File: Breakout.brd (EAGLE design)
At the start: 42 x 45 mm, 11 parts

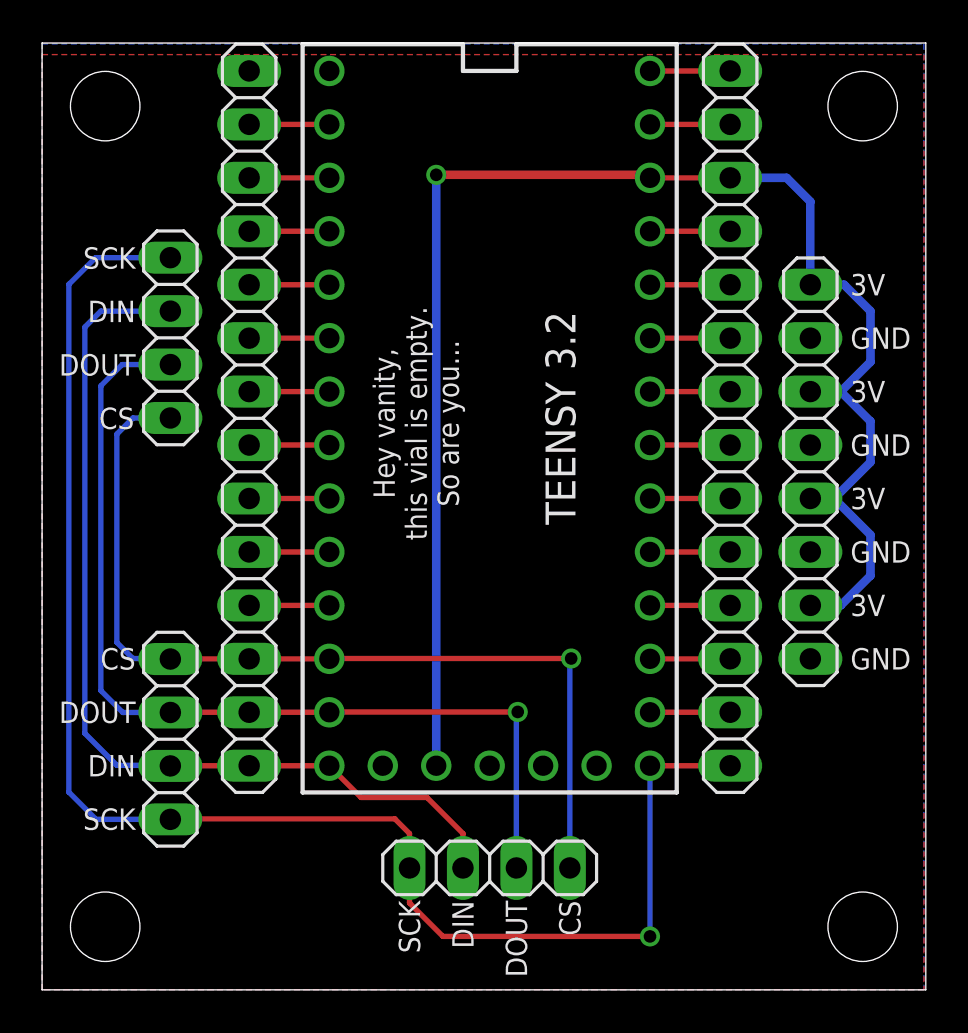
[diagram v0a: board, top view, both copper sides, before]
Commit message: Nudge layout to fit more squarely on mil grid
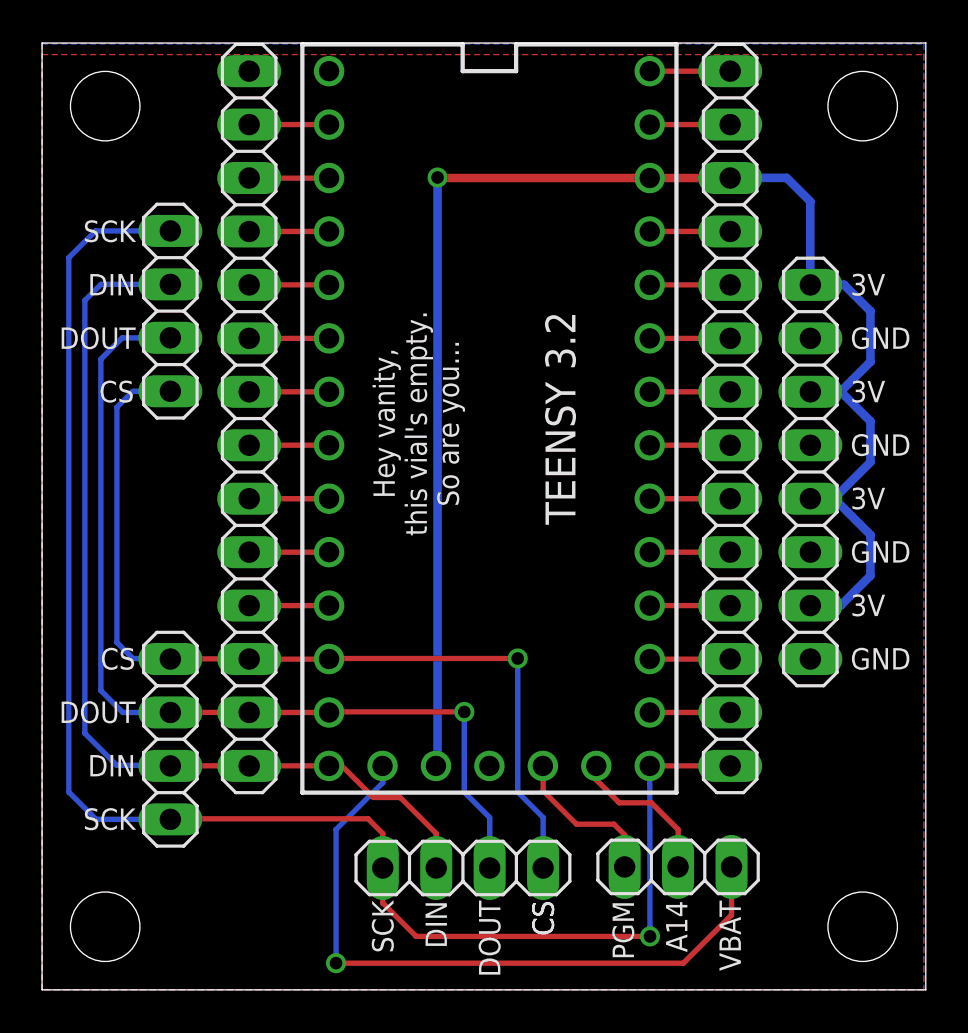
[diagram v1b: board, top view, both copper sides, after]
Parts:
- added JP7: (no value), pinhead:1X03
- moved JP5 1.27 mm to (20.0, 5.79)
- moved JP4 1.27 mm to (6.10, 32.3)
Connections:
- net A14: now also JP7.2
- net PGM: now also JP7.1
- net VBAT: now also JP7.3
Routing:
- net VBAT: track 0.00 -> 32.3 mm, vias 0 -> 1
- net PGM: track 0.00 -> 7.45 mm
- net A14: track 0.00 -> 7.30 mm
- net SCK: track 73.8 -> 75.1 mm
- net DOUT: track 45.9 -> 45.1 mm
- net CS: track 44.7 -> 43.9 mm
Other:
- board text added: "A14"
- board text added: "Hey vanity, this vial's empty. So are you..."
- board text added: "PGM"
- board text added: "VBAT"
- board text removed: "Hey vanity, this vial is empty. So are you..."

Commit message: Add ALL the GNDs...
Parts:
- added JP8: (no value), pinhead:1X03
- JP6: device pinhead:1X08 -> pinhead:1X10
- moved JP4 7.62 mm to (6.10, 24.6)
- moved JP5 3.81 mm to (16.2, 5.79)
- moved JP7 2.54 mm to (27.7, 5.84)
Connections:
- net 3V: now also JP6.9
- net GND: now also JP6.10, JP8.1, JP8.2, JP8.3
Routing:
- net VBAT: track 32.3 -> 17.8 mm, vias 1 -> 0
- net DOUT: track 45.1 -> 34.4 mm
- net CS: track 43.9 -> 33.2 mm
- net DIN: track 45.3 -> 35.0 mm
- net 3V: track 74.8 -> 83.5 mm
- net SCK: track 75.1 -> 67.5 mm
- net PGM: track 7.45 -> 5.36 mm
- net A14: track 7.30 -> 5.36 mm
